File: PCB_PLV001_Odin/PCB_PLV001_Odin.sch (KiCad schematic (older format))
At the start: 11 parts, among them J1 PWR/CAN/QB, U7 R-78B12-2.0

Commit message: Work on Odin and Yggdrasil, create Heimdal.
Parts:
- removed JP1: CAN_TERM, symbol Device:Jumper_NC_Small
- removed R13: 120, symbol Device:R_US
- added C?: 0.1uF, symbol Device:C
- added JP?: CAN_TERM, symbol Device:Jumper_NC_Small
- added R?: 120, symbol Device:R_US
- added U?: SN65HVD232, Package_SO:SOIC-8_3.9x4.9mm_P1.27mm, symbol Interface_CAN_LIN:SN65HVD232
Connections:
- net +3V3: now also C?.1, U?.3 (VCC)
- net CANH: now also R?.1, U?.7 (CANH)
- net CANL: now also JP?.2, U?.6 (CANL)
- net CAN_RX: now also U?.4 (R)
- net CAN_TX: now also U?.1 (D)
- net GND: now also C?.2, U?.2 (GND)
- new net: JP?.1, R?.2
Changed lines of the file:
@@
 F7 "232_2_VALID" O L 7100 1750 50
 F8 "232_1_VALID" O L 7100 1300 50
-F9 "CAN_RX" O R 9000 1000 50
-F10 "CAN_TX" I R 9000 1100 50
-F11 "CANH" B R 9000 1250 50
-F12 "CANL" B R 9000 1350 50
-F13 "UART2_RX" O L 7100 1550 50
+F9 "UART2_RX" O L 7100 1550 50
+F10 "INS_PPS" O R 9000 1000 50
+F11 "IMU_TOV" O R 9000 1100 50
 $EndSheet
 Text Notes 7500 2000 0    118  ~ 0
 Transceivers
-Text Label 9250 1250 2    50   ~ 0
-CANH
-Text Label 9250 1350 2    50   ~ 0
-CANL
-Text Label 9300 1000 2    50   ~ 0
-CAN_RX
-Wire Wire Line
-	9300 1000 9000 1000
-Text Label 9300 1100 2    50   ~ 0
-CAN_TX
-Wire Wire Line
-	9300 1100 9000 1100
 Text Notes 3900 3300 0    50   ~ 0
 Using Nucleo 5V and 3.3V regulation\nMax current 800mA on 5V?\n500mA on 3.3V
@@
 Text Label 6600 1750 0    50   ~ 0
 232_2_VALID
-$Comp
-L Device:R_US R13
-U 1 1 5FC66E65
-P 9500 1250
-F 0 "R13" V 9705 1250 50  0000 C CNN
-F 1 "120" V 9614 1250 50  0000 C CNN
-F 2 "" V 9540 1240 50  0001 C CNN
-F 3 "~" H 9500 1250 50  0001 C CNN
-	1    9500 1250
-	0    -1   -1   0
-$EndComp
-Wire Wire Line
-	9000 1250 9350 1250
-$Comp
-L Device:Jumper_NC_Small JP1
-U 1 1 5FC6A2D3
-P 9850 1250
-F 0 "JP1" H 9850 1462 50  0000 C CNN
-F 1 "CAN_TERM" H 9850 1371 50  0000 C CNN
-F 2 "" H 9850 1250 50  0001 C CNN
-F 3 "~" H 9850 1250 50  0001 C CNN
-	1    9850 1250
-	1    0    0    -1
-$EndComp
-Wire Wire Line
-	9650 1250 9750 1250
-Wire Wire Line
-	10000 1350 10000 1250
-Wire Wire Line
-	10000 1250 9950 1250
-Wire Wire Line
-	9000 1350 10000 1350
 Text Label 6050 1550 2    50   ~ 0
 HEARTBEAT_BUFF
@@
 Text Label 1600 1850 2    50   ~ 0
 VIN
+$Comp
+L Interface_CAN_LIN:SN65HVD232 U?
+U 1 1 5FB5351D
+P 7750 5300
+AR Path="/5FB797DD/5FB5351D" Ref="U?"  Part="1"
+AR Path="/5FB5351D" Ref="U?"  Part="1"
+F 0 "U?" H 7500 5550 50  0000 C CNN
+F 1 "SN65HVD232" H 7400 4950 50  0000 C CNN
+F 2 "Package_SO:SOIC-8_3.9x4.9mm_P1.27mm" H 7750 4800 50  0001 C CNN
+F 3 "http://www.ti.com/lit/ds/symlink/sn65hvd230.pdf" H 7650 5700 50  0001 C CNN
+	1    7750 5300
+	1    0    0    -1
+$EndComp
+$Comp
+L power:+3.3V #PWR?
+U 1 1 5FB5352B
+P 7750 4950
+AR Path="/5FB797DD/5FB5352B" Ref="#PWR?"  Part="1"
+AR Path="/5FB5352B" Ref="#PWR?"  Part="1"
+F 0 "#PWR?" H 7750 4800 50  0001 C CNN
+F 1 "+3.3V" H 7765 5123 50  0000 C CNN
+F 2 "" H 7750 4950 50  0001 C CNN
+F 3 "" H 7750 4950 50  0001 C CNN
+	1    7750 4950
+	1    0    0    -1
+$EndComp
+Wire Wire Line
+	7750 4950 7750 5000
+Wire Wire Line
+	7750 5700 7750 5750
+$Comp
+L power:GND #PWR?
+U 1 1 5FB53533
+P 7750 5750
+AR Path="/5FB53533" Ref="#PWR?"  Part="1"
+AR Path="/5FB797DD/5FB53533" Ref="#PWR?"  Part="1"
+F 0 "#PWR?" H 7750 5500 50  0001 C CNN
+F 1 "GND" H 7755 5577 50  0000 C CNN
+F 2 "" H 7750 5750 50  0001 C CNN
+F 3 "" H 7750 5750 50  0001 C CNN
+	1    7750 5750
+	1    0    0    -1
+$EndComp
+$Comp
+L Device:C C?
+U 1 1 5FB53539
+P 9400 5350
+AR Path="/5FB53539" Ref="C?"  Part="1"
+AR Path="/5FB797DD/5FB53539" Ref="C?"  Part="1"
+F 0 "C?" H 9515 5396 50  0000 L CNN
+F 1 "0.1uF" H 9515 5305 50  0000 L CNN
+F 2 "" H 9438 5200 50  0001 C CNN
+F 3 "~" H 9400 5350 50  0001 C CNN
+	1    9400 5350
+	1    0    0    -1
+$EndComp
+$Comp
+L power:GND #PWR?
+U 1 1 5FB5353F
+P 9400 5550
+AR Path="/5FB5353F" Ref="#PWR?"  Part="1"
+AR Path="/5FB797DD/5FB5353F" Ref="#PWR?"  Part="1"
+F 0 "#PWR?" H 9400 5300 50  0001 C CNN
+F 1 "GND" H 9405 5377 50  0000 C CNN
+F 2 "" H 9400 5550 50  0001 C CNN
+F 3 "" H 9400 5550 50  0001 C CNN
+	1    9400 5550
+	1    0    0    -1
+$EndComp
+Wire Wire Line
+	9400 5500 9400 5550
+$Comp
+L power:+3.3V #PWR?
+U 1 1 5FB53546
+P 9400 5150
+AR Path="/5FB53546" Ref="#PWR?"  Part="1"
+AR Path="/5FB797DD/5FB53546" Ref="#PWR?"  Part="1"
+F 0 "#PWR?" H 9400 5000 50  0001 C CNN
+F 1 "+3.3V" H 9415 5323 50  0000 C CNN
+F 2 "" H 9400 5150 50  0001 C CNN
+F 3 "" H 9400 5150 50  0001 C CNN
+	1    9400 5150
+	1    0    0    -1
+$EndComp
+Wire Wire Line
+	9400 5150 9400 5200
+Text Label 7050 5200 0    50   ~ 0
+CAN_TX
+Wire Wire Line
+	7050 5200 7350 5200
+Text Label 7050 5300 0    50   ~ 0
+CAN_RX
+Wire Wire Line
+	7050 5300 7350 5300
+Text Label 8400 5300 2    50   ~ 0
+CANH
+Text Label 8400 5400 2    50   ~ 0
+CANL
+$Comp
+L Device:R_US R?
+U 1 1 5FB5AB7E
+P 8650 5300
+F 0 "R?" V 8855 5300 50  0000 C CNN
+F 1 "120" V 8764 5300 50  0000 C CNN
+F 2 "" V 8690 5290 50  0001 C CNN
+F 3 "~" H 8650 5300 50  0001 C CNN
+	1    8650 5300
+	0    -1   -1   0
+$EndComp
+$Comp
+L Device:Jumper_NC_Small JP?
+U 1 1 5FB5AB89
+P 9000 5300
+F 0 "JP?" H 9000 5512 50  0000 C CNN
+F 1 "CAN_TERM" H 9000 5421 50  0000 C CNN
+F 2 "" H 9000 5300 50  0001 C CNN
+F 3 "~" H 9000 5300 50  0001 C CNN
+	1    9000 5300
+	1    0    0    -1
+$EndComp
+Wire Wire Line
+	8800 5300 8900 5300
+Wire Wire Line
+	9150 5400 9150 5300
+Wire Wire Line
+	9150 5300 9100 5300
+Wire Wire Line
+	8150 5400 9150 5400
+Wire Wire Line
+	8150 5300 8500 5300
 $EndSCHEMATC

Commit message: Odin initial schematics ready for review
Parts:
- added C23: 10uF, symbol Device:C
- added C24, C25: 1uF, symbol Device:C
- added C26, C28, C29: 0.1uF, symbol Device:C
- added J4: ROT1, symbol Connector_Generic:Conn_01x06
- added J5: ROT2, symbol Connector_Generic:Conn_01x06
- added R13, R26, R27, R28: 0, symbol Device:R_US
- added R29, R30, R31, R32, R33, R34, R35, R36, R37, R38: 10K, symbol Device:R_US
- gave numbers to parts that had none: 6
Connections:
- net +12V: now also C23.1, C24.1, C25.1, C26.1
- net +3V3: now also C28.1, C29.1
- net +5V: now also R13.2, R26.2, R27.2, R28.2, R29.2, R30.2, R31.2, R32.2, R33.2, R34.2, R35.2, R36.2, R37.2, R38.2
- net AvionicsHeartbeatTemplate/HEARTBEAT_INPUT_4: now also R13.1
- net AvionicsHeartbeatTemplate/HEARTBEAT_INPUT_5: now also R26.1
- net CAN_RX: no longer NCLO1.50 (PA12/CAN1_TD/UART1_RTS)
- net CAN_TX: now also NCLO1.50 (PA12/CAN1_TD/UART1_RTS)
- net GND: now also C23.2, C24.2, C25.2, C26.2, C28.2, C29.2, J4.1 (Pin_1), J5.1 (Pin_1)
- net UART1_RX: no longer NCLO1.75 (PA3/UART2_RX)
- net UART1_TX: no longer NCLO1.73 (PA2/UART2_TX)
- net INS_PPS: now reaches NCLO1.13 (PA13)
- net IMU_TOV: now reaches NCLO1.15 (PA14)
- net ROT2_PPS3: now reaches NCLO1.21 (PB7/I2C1_SDA/PWM4_2/UART1_RX)
- net ROT2_PPS3: now also J5.4 (Pin_4), R36.1
- net n232_1_EN: now reaches NCLO1.25 (PC14)
- net n232_2_EN: now reaches NCLO1.27 (PC15)
- net MCU_QB_INPUT: now reaches NCLO1.30 (PA1/ADC/PWM2_2/UART2_RTS/UART4_RX)
- net HEARTBEAT_RESTART: now reaches NCLO1.32 (PA4/ADC/SPI1_SSEL/DAC)
- net ROT1_PPS5: now reaches NCLO1.34 (PB0/ADC/PWM3_3)
- net ROT1_PPS5: now also J4.6 (Pin_6), R29.1
- net ROT2_PPS2: now reaches NCLO1.41 (PB8/CAN1_RD/I2C1_SCL/PWM4_3)
- net ROT2_PPS2: now also J5.3 (Pin_3), R37.1
- net ROT2_PPS1: now reaches NCLO1.43 (PB9/SPI2_SSEL/CAN1_TD/I2C1_SDA/PWM4_4)
- net ROT2_PPS1: now also J5.2 (Pin_2), R38.1
- net UART2_RX: now reaches NCLO1.44 (PC5/ADC/UART3_RX)
- net ROT2_PPS4: now reaches NCLO1.55 (PB6/I2C1_SCL/UART1_TX/PWM4_1)
- net ROT2_PPS4: now also J5.5 (Pin_5), R35.1
- net ROT1_PPS3: now reaches NCLO1.60 (PB2)
- net ROT1_PPS3: now also J4.4 (Pin_4), R31.1
- net ROT1_PPS4: now reaches NCLO1.62 (PB1/ADC/PWM3_4)
- net ROT1_PPS4: now also J4.5 (Pin_5), R30.1
- net ROT1_PPS1: now reaches NCLO1.65 (PB4/SPI1_MISO/PWM3_1)
- net ROT1_PPS1: now also J4.2 (Pin_2), R33.1
- net ROT2_PPS5: now reaches NCLO1.67 (PB5/SPI1_MOSI/PWM3_2)
- net ROT2_PPS5: now also J5.6 (Pin_6), R34.1
- net ROT1_PPS2: now reaches NCLO1.69 (PB3/SPI1_SCLK/PWM2_2)
- net ROT1_PPS2: now also J4.3 (Pin_3), R32.1
- net UART2_TX: now reaches NCLO1.72 (PC4/ADC/UART3_TX)
- new net AvionicsHeartbeatTemplate/HEARTBEAT_INPUT_6: R27.1
- new net AvionicsHeartbeatTemplate/HEARTBEAT_INPUT_7: R28.1
- no-connect marks 7 -> 37
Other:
- note removed: "TODO:\n-Rotary sensors\n-MCU heartbeat inputs"
- moved on the sheet: C10, C27, C8, C9, FB1, JP1, NCLO1, R39, U10, U7

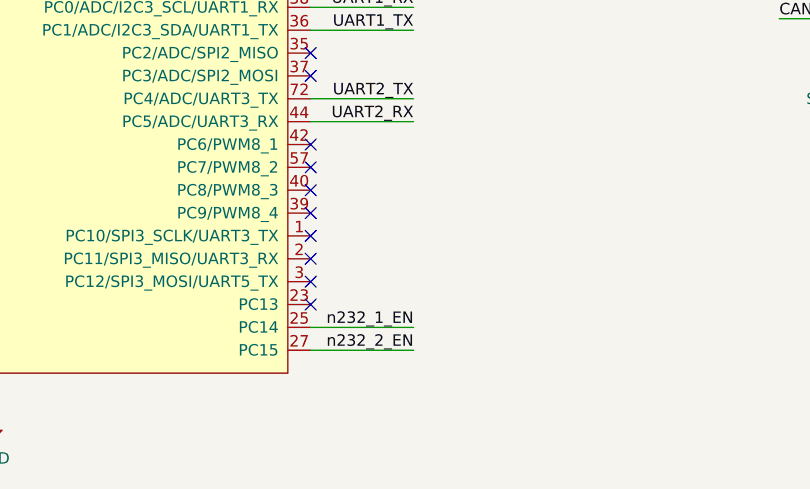
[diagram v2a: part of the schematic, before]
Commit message: Add heartbeat address lines to uC GPIO
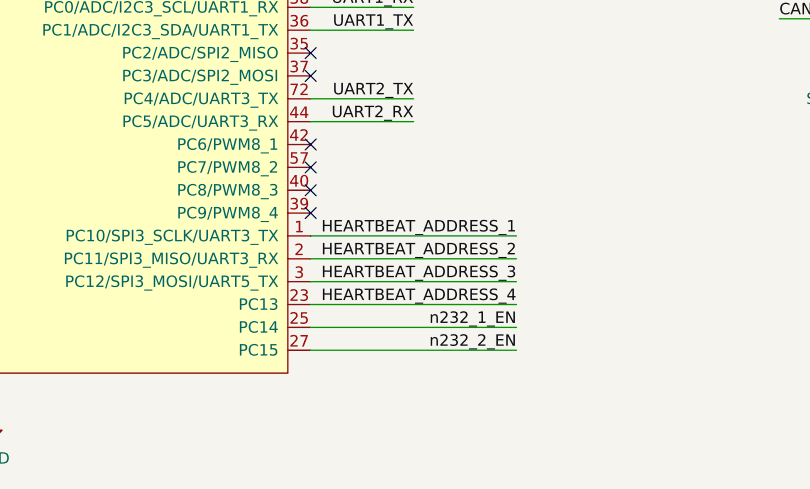
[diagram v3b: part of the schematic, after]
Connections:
- net HEARTBEAT_ADDRESS_1: now also NCLO1.1 (PC10/SPI3_SCLK/UART3_TX)
- net HEARTBEAT_ADDRESS_2: now also NCLO1.2 (PC11/SPI3_MISO/UART3_RX)
- net HEARTBEAT_ADDRESS_3: now also NCLO1.3 (PC12/SPI3_MOSI/UART5_TX)
- net HEARTBEAT_ADDRESS_4: now also NCLO1.23 (PC13)
- no-connect marks 37 -> 33
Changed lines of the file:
@@
 Wire Wire Line
 	7250 1550 7750 1550
-Text Label 5550 7350 2    50   ~ 0
+Text Label 6000 7350 2    50   ~ 0
 n232_1_EN
 Wire Wire Line
-	5550 7350 5100 7350
-Wire Wire Line
-	5100 7450 5550 7450
-Text Label 5550 7450 2    50   ~ 0
+	6000 7350 5100 7350
+Wire Wire Line
+	5100 7450 6000 7450
+Text Label 6000 7450 2    50   ~ 0
 n232_2_EN
 Text Label 10050 900  2    50   ~ 0
@@
 NoConn ~ 5100 6750
 NoConn ~ 5100 6850
-NoConn ~ 5100 6950
-NoConn ~ 5100 7050
-NoConn ~ 5100 7150
-NoConn ~ 5100 7250
 NoConn ~ 1500 5450
 NoConn ~ 1500 4950
@@
 Text Label 7000 1200 2    50   ~ 0
 HEARTBEAT_ADDRESS_4
+Wire Wire Line
+	5100 7150 6000 7150
+Wire Wire Line
+	6000 7050 5100 7050
+Wire Wire Line
+	5100 6950 6000 6950
+Text Label 6000 6950 2    50   ~ 0
+HEARTBEAT_ADDRESS_1
+Text Label 6000 7050 2    50   ~ 0
+HEARTBEAT_ADDRESS_2
+Text Label 6000 7150 2    50   ~ 0
+HEARTBEAT_ADDRESS_3
+Text Label 6000 7250 2    50   ~ 0
+HEARTBEAT_ADDRESS_4
+Wire Wire Line
+	6000 7250 5100 7250
 $EndSCHEMATC

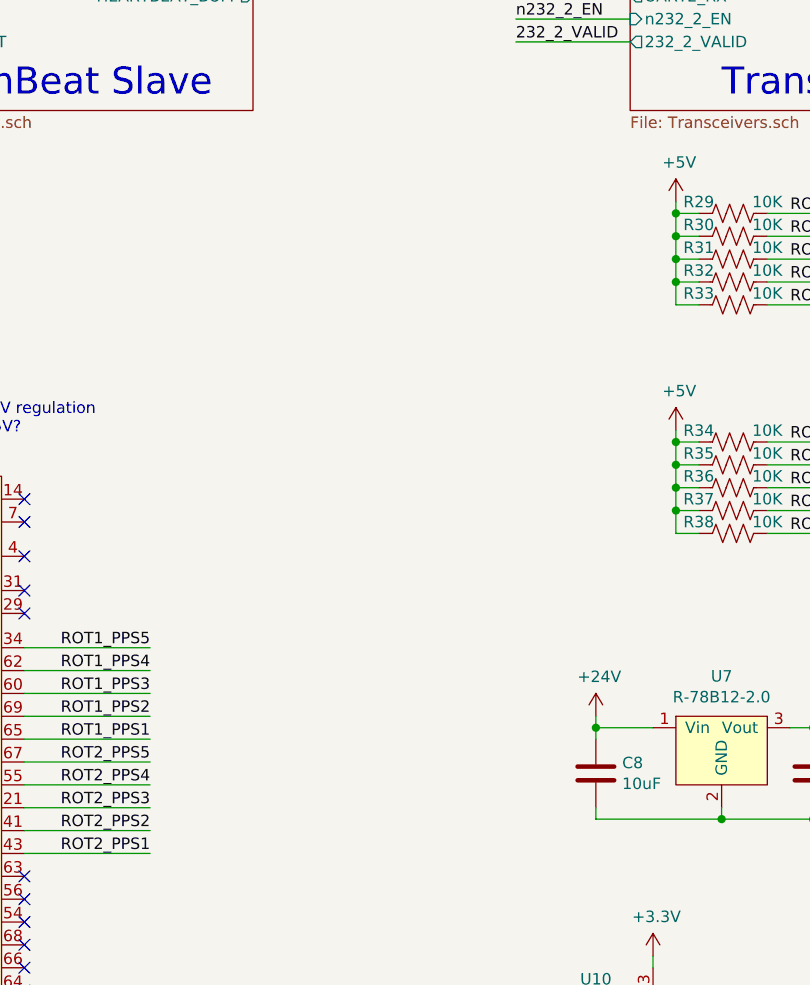
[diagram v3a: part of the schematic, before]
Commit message: Add power LEDs and large input caps to Yggdrasil, Odin
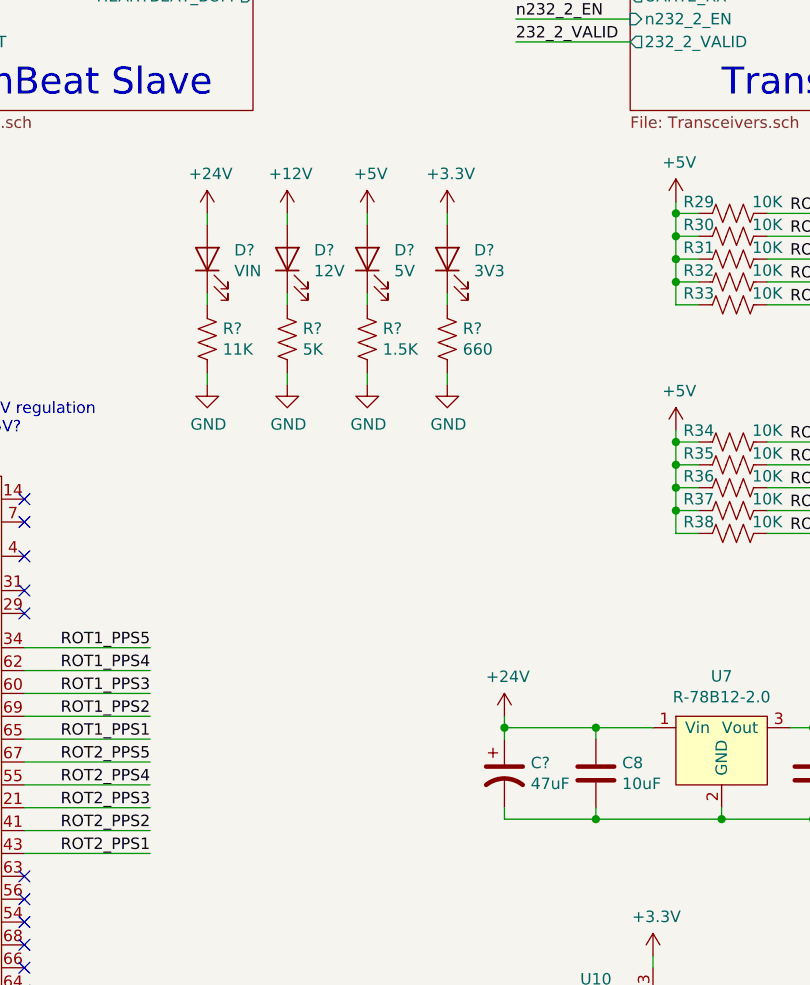
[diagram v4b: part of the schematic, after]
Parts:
- added C?: 47uF, symbol Device:CP1
- added D?: VIN, symbol Device:LED
- added D?: 12V, symbol Device:LED
- added D?: 5V, symbol Device:LED
- added D?: 3V3, symbol Device:LED
- added R?: 11K, symbol Device:R_US
- added R?: 5K, symbol Device:R_US
- added R?: 1.5K, symbol Device:R_US
- added R?: 660, symbol Device:R_US
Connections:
- net +12V: now also D?.2 (A)
- net +24V: now also C?.1, D?.2 (A)
- net +3V3: now also D?.2 (A)
- net +5V: now also D?.2 (A)
- net GND: now also C?.2, R?.2, R?.2, R?.2, R?.2
- new net: D?.1 (K), R?.1 (x4)

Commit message: Spec all current parts for Odin
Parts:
- removed C10, C27, C28, C29: 0.1uF, symbol Device:C
- removed C8: 10uF, symbol Device:C
- removed R30, R31, R32, R33: 10K, symbol Device:R_US
- added C1, C2, C3, C4: 0.1uF, Capacitor_SMD:C_0603_1608Metric_Pad1.05x0.95mm_HandSolder, symbol Device:C
- added C30: 10uF, Capacitor_SMD:C_1210_3225Metric_Pad1.42x2.65mm_HandSolder, symbol Device:C
- added R40, R41, R42, R43: 10K, Resistor_SMD:R_0603_1608Metric_Pad1.05x0.95mm_HandSolder, symbol Device:R_US
- C23, C9: footprint (none) -> Capacitor_SMD:C_1210_3225Metric_Pad1.42x2.65mm_HandSolder; MFPN (none) -> GRM32EC72A106KE05L
- C24, C25: value 1uF -> 10uF; footprint (none) -> Capacitor_SMD:C_1210_3225Metric_Pad1.42x2.65mm_HandSolder; MFPN (none) -> GRM32EC72A106KE05L
- C26: value 0.1uF -> 10uF; footprint (none) -> Capacitor_SMD:C_1210_3225Metric_Pad1.42x2.65mm_HandSolder; MFPN (none) -> GRM32EC72A106KE05L
- C8: renamed from C?; footprint (none) -> Capacitor_THT:CP_Radial_D6.3mm_P2.50mm; MFPN (none) -> UVR1H470MED
- D1: footprint (none) -> BoringFootprints:DO-221AC; MFPN (none) -> VSSAF5N50-M3/6A
- D4, D5, D6, D7: renamed from D?; footprint (none) -> LED_SMD:LED_0805_2012Metric_Pad1.15x1.40mm_HandSolder; MFPN (none) -> 150080GS75000
- F1: footprint (none) -> BoringFootprints:BelFuse_0679H; MFPN (none) -> 0679H2000-05
- FB1: value Ferrite_Bead -> 30ohm@100MHz; footprint (none) -> Inductor_SMD:L_0805_2012Metric_Pad1.15x1.40mm_HandSolder; MFPN (none) -> BLM21SN300SH1D
- J1: footprint (none) -> Connector_Molex:Molex_Micro-Fit_3.0_43045-1200_2x06_P3.00mm_Horizontal; MFPN (none) -> 0430451200
- J4, J5: footprint (none) -> Connector_Molex:Molex_Micro-Fit_3.0_43045-0600_2x03_P3.00mm_Horizontal; MFPN (none) -> 0430450600
- JP1: footprint (none) -> Jumper:SolderJumper-2_P1.3mm_Open_RoundedPad1.0x1.5mm
- R13, R26, R27, R28: footprint (none) -> Resistor_SMD:R_0603_1608Metric_Pad1.05x0.95mm_HandSolder
- R29, R34, R35, R36, R37, R38: footprint (none) -> Resistor_SMD:R_0603_1608Metric_Pad1.05x0.95mm_HandSolder; MFPN (none) -> RMCF0603FT10K0
- R30: renamed from R?; footprint (none) -> Resistor_SMD:R_0603_1608Metric_Pad1.05x0.95mm_HandSolder; MFPN (none) -> RMCF0603FT11K0
- R31: renamed from R?; value 5K -> 4.7K; footprint (none) -> Resistor_SMD:R_0603_1608Metric_Pad1.05x0.95mm_HandSolder; MFPN (none) -> RMCF0603FT4K70
- R32: renamed from R?; value 1.5K -> 1K; footprint (none) -> Resistor_SMD:R_0603_1608Metric_Pad1.05x0.95mm_HandSolder; MFPN (none) -> RMCF0603FT1K00
- R33: renamed from R?; value 660 -> 47; footprint (none) -> Resistor_SMD:R_0603_1608Metric_Pad1.05x0.95mm_HandSolder; MFPN (none) -> RMCF0603FT47R0
- R39: footprint (none) -> Resistor_SMD:R_1210_3225Metric_Pad1.42x2.65mm_HandSolder; MFPN (none) -> RMCF1210FT120R
- U10: MFPN (none) -> SN65HVD232QDRQ1
- U7: MFPN (none) -> R-78B12-2.0
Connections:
- net +12V: now also C1.1
- net +24V: now also C9.1
- net +3V3: now also C2.1, C3.1, C4.1
- net +5V: now also R40.2, R41.2, R42.2, R43.2
- net GND: now also C1.2, C2.2, C3.2, C30.2, C4.2
- net ROT1_PPS1: now also R37.1
- net ROT1_PPS2: now also R36.1
- net ROT1_PPS3: now also R35.1
- net ROT1_PPS4: now also R34.1
- net ROT2_PPS1: now also R43.1; no longer R38.1
- net ROT2_PPS2: now also R42.1; no longer R37.1
- net ROT2_PPS3: now also R41.1; no longer R36.1
- net ROT2_PPS4: now also R40.1; no longer R35.1
- net ROT2_PPS5: now also R38.1; no longer R34.1
- net at FB1.2, U7.3 (Vout): now also C30.1; no longer C9.1
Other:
- note added: "NOTE: Give this diode a big pad for heat"
- moved on the sheet: FB1
